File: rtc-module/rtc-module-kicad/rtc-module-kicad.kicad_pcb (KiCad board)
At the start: 2 copper layers, 45.5 x 36.4 mm, 11 parts, among them J1 Battery-holder, J2 Microcontroller, U1 PCF8563T

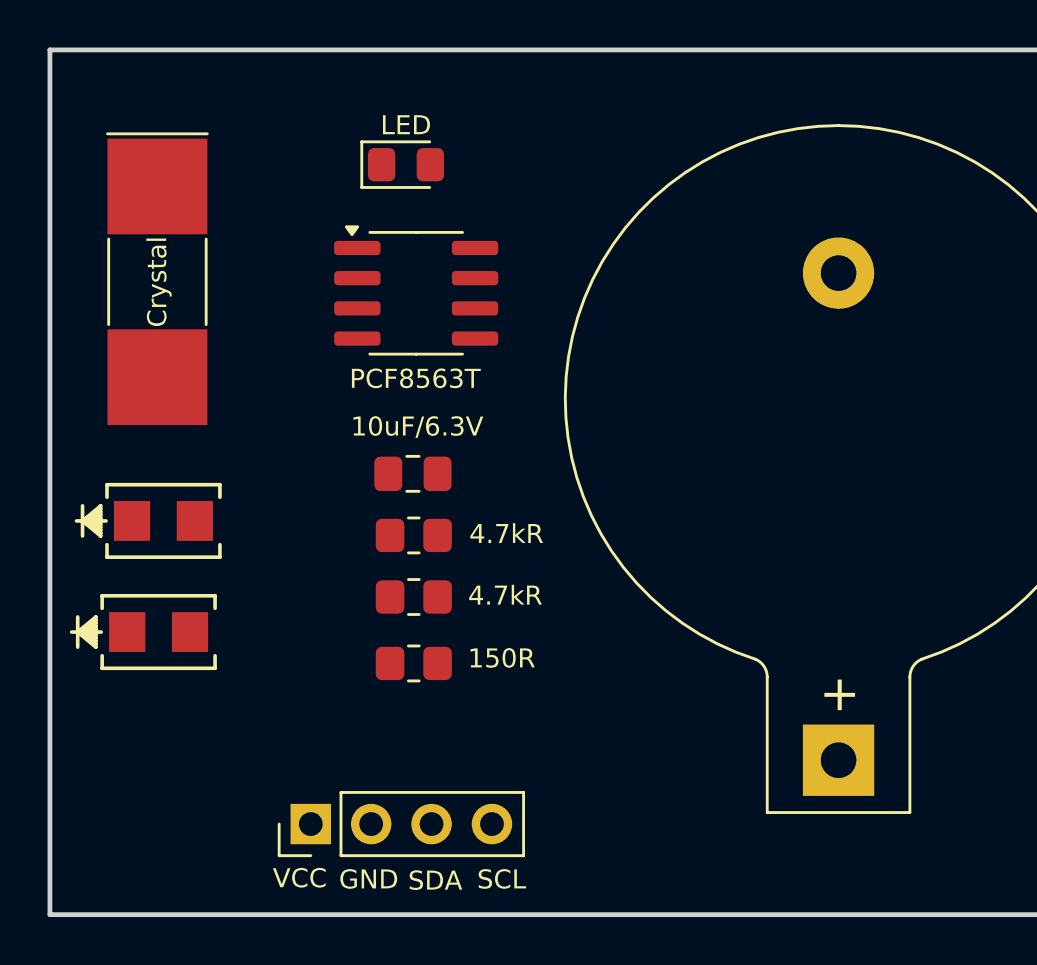
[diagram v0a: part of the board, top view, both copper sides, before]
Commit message: Connected items on the pcb.
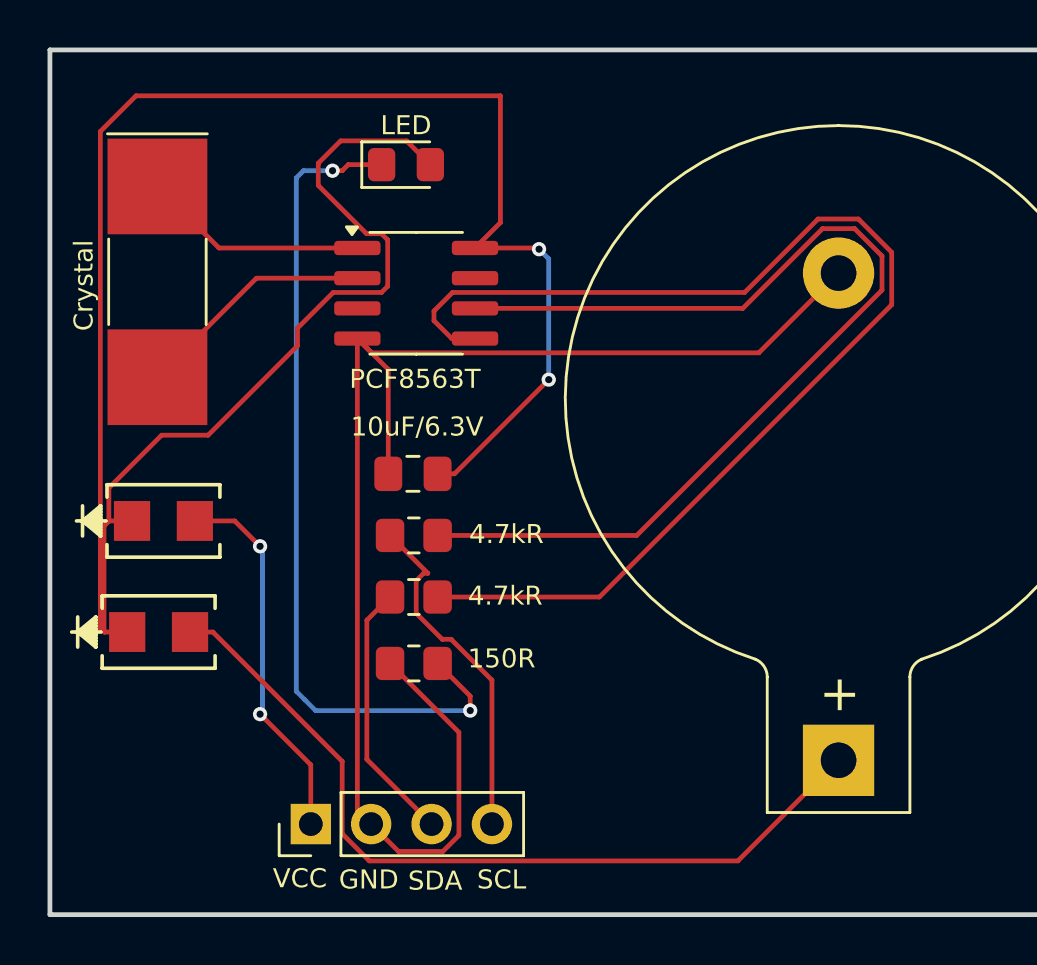
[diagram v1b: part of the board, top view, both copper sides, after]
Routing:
- net Net-(D1-K): track 0.00 -> 96.1 mm, vias 0 -> 2
- net Net-(J1-Pin_2): track 0.00 -> 61.6 mm
- net Net-(U1-SDA): track 0.00 -> 50.3 mm
- net Net-(U1-SCL): track 0.00 -> 43.4 mm
- net Net-(D3-K): track 0.00 -> 35.6 mm, vias 0 -> 2
- net Net-(D1-A): track 0.00 -> 34.8 mm
- net Net-(D2-A): track 0.00 -> 15.8 mm, vias 0 -> 2
- net Net-(J2-Pin_4): track 0.00 -> 14.6 mm
- net Net-(J2-Pin_3): track 0.00 -> 11.1 mm
- net Net-(U1-OSCO): track 0.00 -> 10.1 mm
- net Net-(U1-OSCI): track 0.00 -> 9.48 mm

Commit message: Added the gerber and drill files ready to order!
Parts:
- added 10uF/6.3V: C - 10uF/6.3V, Capacitor_SMD:C_0805_2012Metric_Pad1.18x1.45mm_HandSolder, F.Cu at (126.1, 164.4)
- added 10uF/6.3V: C - 10uF/6.3V, Capacitor_SMD:C_0805_2012Metric_Pad1.18x1.45mm_HandSolder, F.Cu at (77.9, 125.2)
- added 10uF/6.3V: C - 10uF/6.3V, Capacitor_SMD:C_0805_2012Metric_Pad1.18x1.45mm_HandSolder, F.Cu at (77.7, 86.4)
- added 10uF/6.3V: C - 10uF/6.3V, Capacitor_SMD:C_0805_2012Metric_Pad1.18x1.45mm_HandSolder, F.Cu at (125.8, 86.9)
- added 10uF/6.3V: C - 10uF/6.3V, Capacitor_SMD:C_0805_2012Metric_Pad1.18x1.45mm_HandSolder, F.Cu at (126.0, 125.6)
- added 10uF/6.3V: C - 10uF/6.3V, Capacitor_SMD:C_0805_2012Metric_Pad1.18x1.45mm_HandSolder, F.Cu at (125.7, 48.1)
- added 10uF/6.3V: C - 10uF/6.3V, Capacitor_SMD:C_0805_2012Metric_Pad1.18x1.45mm_HandSolder, F.Cu at (77.6, 47.7)
- added 150R: 150R, Resistor_SMD:R_0805_2012Metric_Pad1.20x1.40mm_HandSolder, F.Cu at (77.6, 55.6)
- added 150R: 150R, Resistor_SMD:R_0805_2012Metric_Pad1.20x1.40mm_HandSolder, F.Cu at (125.7, 56.1)
- added 150R: 150R, Resistor_SMD:R_0805_2012Metric_Pad1.20x1.40mm_HandSolder, F.Cu at (126.0, 133.6)
- added 150R: 150R, Resistor_SMD:R_0805_2012Metric_Pad1.20x1.40mm_HandSolder, F.Cu at (77.9, 133.1)
- added 150R: 150R, Resistor_SMD:R_0805_2012Metric_Pad1.20x1.40mm_HandSolder, F.Cu at (77.7, 94.4)
- added 150R: 150R, Resistor_SMD:R_0805_2012Metric_Pad1.20x1.40mm_HandSolder, F.Cu at (125.8, 94.8)
- added 150R: 150R, Resistor_SMD:R_0805_2012Metric_Pad1.20x1.40mm_HandSolder, F.Cu at (126.2, 172.4)
- added Crystal: Crystal - 32.768kHz, Crystal:Crystal_SMD_MicroCrystal_CC1V-T1A-2Pin_8.0x3.7mm_HandSoldering, F.Cu at (115.2, 117.6)
- added Crystal: Crystal - 32.768kHz, Crystal:Crystal_SMD_MicroCrystal_CC1V-T1A-2Pin_8.0x3.7mm_HandSoldering, F.Cu at (115.4, 156.3)
- added Crystal: Crystal - 32.768kHz, Crystal:Crystal_SMD_MicroCrystal_CC1V-T1A-2Pin_8.0x3.7mm_HandSoldering, F.Cu at (66.8, 39.6)
- added Crystal: Crystal - 32.768kHz, Crystal:Crystal_SMD_MicroCrystal_CC1V-T1A-2Pin_8.0x3.7mm_HandSoldering, F.Cu at (115.1, 78.8)
- added Crystal: Crystal - 32.768kHz, Crystal:Crystal_SMD_MicroCrystal_CC1V-T1A-2Pin_8.0x3.7mm_HandSoldering, F.Cu at (67.0, 78.3)
- added Crystal: Crystal - 32.768kHz, Crystal:Crystal_SMD_MicroCrystal_CC1V-T1A-2Pin_8.0x3.7mm_HandSoldering, F.Cu at (67.1, 117.1)
- added Crystal: Crystal - 32.768kHz, Crystal:Crystal_SMD_MicroCrystal_CC1V-T1A-2Pin_8.0x3.7mm_HandSoldering, F.Cu at (114.9, 40.0)
- added D1: Schottky-diode, SS14_Schottky:DO-214AC_VIS, F.Cu at (67.0, 93.1)
- added D1: Schottky-diode, SS14_Schottky:DO-214AC_VIS, F.Cu at (66.9, 54.3)
- added D1: Schottky-diode, SS14_Schottky:DO-214AC_VIS, F.Cu at (115.1, 93.5)
- added D1: Schottky-diode, SS14_Schottky:DO-214AC_VIS, F.Cu at (115.4, 171.0)
- added D1: Schottky-diode, SS14_Schottky:DO-214AC_VIS, F.Cu at (115.0, 54.8)
- added D1: Schottky-diode, SS14_Schottky:DO-214AC_VIS, F.Cu at (67.2, 131.8)
- added D1: Schottky-diode, SS14_Schottky:DO-214AC_VIS, F.Cu at (115.3, 132.3)
- added D2: Schottky-diode, SS14_Schottky:DO-214AC_VIS, F.Cu at (67.4, 127.2)
- added D2: Schottky-diode, SS14_Schottky:DO-214AC_VIS, F.Cu at (115.6, 166.4)
- added D2: Schottky-diode, SS14_Schottky:DO-214AC_VIS, F.Cu at (67.2, 88.4)
- added D2: Schottky-diode, SS14_Schottky:DO-214AC_VIS, F.Cu at (67.1, 49.6)
- added D2: Schottky-diode, SS14_Schottky:DO-214AC_VIS, F.Cu at (115.5, 127.6)
- added D2: Schottky-diode, SS14_Schottky:DO-214AC_VIS, F.Cu at (115.3, 88.8)
- added D2: Schottky-diode, SS14_Schottky:DO-214AC_VIS, F.Cu at (115.2, 50.1)
- added J1: Battery-holder, Battery:BatteryHolder_Keystone_103_1x20mm, F.Cu at (143.7, 98.9)
- added J1: Battery-holder, Battery:BatteryHolder_Keystone_103_1x20mm, F.Cu at (143.9, 137.7)
- added J1: Battery-holder, Battery:BatteryHolder_Keystone_103_1x20mm, F.Cu at (144.0, 176.4)
- added J1: Battery-holder, Battery:BatteryHolder_Keystone_103_1x20mm, F.Cu at (95.8, 137.2)
- added J1: Battery-holder, Battery:BatteryHolder_Keystone_103_1x20mm, F.Cu at (95.6, 98.5)
- added J1: Battery-holder, Battery:BatteryHolder_Keystone_103_1x20mm, F.Cu at (143.6, 60.2)
- added J1: Battery-holder, Battery:BatteryHolder_Keystone_103_1x20mm, F.Cu at (95.5, 59.7)
- added J2: Microcontroller, Connector_PinHeader_2.54mm:PinHeader_1x04_P2.54mm_Vertical, F.Cu at (73.6, 139.9)
- added J2: Microcontroller, Connector_PinHeader_2.54mm:PinHeader_1x04_P2.54mm_Vertical, F.Cu at (121.5, 101.6)
- added J2: Microcontroller, Connector_PinHeader_2.54mm:PinHeader_1x04_P2.54mm_Vertical, F.Cu at (121.4, 62.8)
- added J2: Microcontroller, Connector_PinHeader_2.54mm:PinHeader_1x04_P2.54mm_Vertical, F.Cu at (73.3, 62.4)
- added J2: Microcontroller, Connector_PinHeader_2.54mm:PinHeader_1x04_P2.54mm_Vertical, F.Cu at (121.7, 140.4)
- added J2: Microcontroller, Connector_PinHeader_2.54mm:PinHeader_1x04_P2.54mm_Vertical, F.Cu at (121.8, 179.1)
- added J2: Microcontroller, Connector_PinHeader_2.54mm:PinHeader_1x04_P2.54mm_Vertical, F.Cu at (73.4, 101.1)
- added LED: LED, LED_SMD:LED_0805_2012Metric_Pad1.15x1.40mm_HandSolder, F.Cu at (77.3, 34.6)
- added LED: LED, LED_SMD:LED_0805_2012Metric_Pad1.15x1.40mm_HandSolder, F.Cu at (125.7, 112.6)
- added LED: LED, LED_SMD:LED_0805_2012Metric_Pad1.15x1.40mm_HandSolder, F.Cu at (77.4, 73.4)
- added LED: LED, LED_SMD:LED_0805_2012Metric_Pad1.15x1.40mm_HandSolder, F.Cu at (125.5, 73.9)
- added LED: LED, LED_SMD:LED_0805_2012Metric_Pad1.15x1.40mm_HandSolder, F.Cu at (125.8, 151.4)
- added LED: LED, LED_SMD:LED_0805_2012Metric_Pad1.15x1.40mm_HandSolder, F.Cu at (125.4, 35.1)
- added LED: LED, LED_SMD:LED_0805_2012Metric_Pad1.15x1.40mm_HandSolder, F.Cu at (77.6, 112.2)
- added R1: 4.7kR, Resistor_SMD:R_0805_2012Metric_Pad1.20x1.40mm_HandSolder, F.Cu at (125.7, 53.3)
- added R1: 4.7kR, Resistor_SMD:R_0805_2012Metric_Pad1.20x1.40mm_HandSolder, F.Cu at (77.7, 91.6)
- added R1: 4.7kR, Resistor_SMD:R_0805_2012Metric_Pad1.20x1.40mm_HandSolder, F.Cu at (126.2, 169.6)
- added R1: 4.7kR, Resistor_SMD:R_0805_2012Metric_Pad1.20x1.40mm_HandSolder, F.Cu at (125.8, 92.0)
- added R1: 4.7kR, Resistor_SMD:R_0805_2012Metric_Pad1.20x1.40mm_HandSolder, F.Cu at (77.6, 52.8)
- added R1: 4.7kR, Resistor_SMD:R_0805_2012Metric_Pad1.20x1.40mm_HandSolder, F.Cu at (77.9, 130.4)
- added R1: 4.7kR, Resistor_SMD:R_0805_2012Metric_Pad1.20x1.40mm_HandSolder, F.Cu at (126.0, 130.8)
- added R2: 4.7kR, Resistor_SMD:R_0805_2012Metric_Pad1.20x1.40mm_HandSolder, F.Cu at (77.6, 50.2)
- added R2: 4.7kR, Resistor_SMD:R_0805_2012Metric_Pad1.20x1.40mm_HandSolder, F.Cu at (125.7, 50.7)
- added R2: 4.7kR, Resistor_SMD:R_0805_2012Metric_Pad1.20x1.40mm_HandSolder, F.Cu at (125.8, 89.5)
- added R2: 4.7kR, Resistor_SMD:R_0805_2012Metric_Pad1.20x1.40mm_HandSolder, F.Cu at (77.7, 89.0)
- added R2: 4.7kR, Resistor_SMD:R_0805_2012Metric_Pad1.20x1.40mm_HandSolder, F.Cu at (126.2, 167.0)
- added R2: 4.7kR, Resistor_SMD:R_0805_2012Metric_Pad1.20x1.40mm_HandSolder, F.Cu at (126.0, 128.2)
- added R2: 4.7kR, Resistor_SMD:R_0805_2012Metric_Pad1.20x1.40mm_HandSolder, F.Cu at (77.9, 127.8)
- added U1: PCF8563T, Package_SO:SOIC-8_3.9x4.9mm_P1.27mm, F.Cu at (126.3, 156.8)
- added U1: PCF8563T, Package_SO:SOIC-8_3.9x4.9mm_P1.27mm, F.Cu at (125.8, 40.5)
- added U1: PCF8563T, Package_SO:SOIC-8_3.9x4.9mm_P1.27mm, F.Cu at (78.0, 117.6)
- added U1: PCF8563T, Package_SO:SOIC-8_3.9x4.9mm_P1.27mm, F.Cu at (125.9, 79.3)
- added U1: PCF8563T, Package_SO:SOIC-8_3.9x4.9mm_P1.27mm, F.Cu at (126.1, 118.0)
- added U1: PCF8563T, Package_SO:SOIC-8_3.9x4.9mm_P1.27mm, F.Cu at (77.7, 40.1)
- added U1: PCF8563T, Package_SO:SOIC-8_3.9x4.9mm_P1.27mm, F.Cu at (77.8, 78.8)
- moved D2 82.2 mm to (67.5, 165.9)
- moved R1 82.2 mm to (78.0, 169.1)
- moved R2 82.2 mm to (78.0, 166.5)
- moved 10uF/6.3V 82.2 mm to (78.0, 163.9)
- moved 150R 82.2 mm to (78.0, 171.9)
- moved Crystal 82.2 mm to (67.3, 155.9)
- moved D1 82.2 mm to (67.3, 170.6)
- moved J1 82.2 mm to (95.9, 176.0)
- moved J2 82.2 mm to (73.7, 178.7)
- moved LED 82.2 mm to (77.7, 150.9)
- moved U1 82.2 mm to (78.1, 156.3)
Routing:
- net Net-(D1-K): track 96.1 -> 769.1 mm, vias 2 -> 16
- net Net-(J1-Pin_2): track 61.6 -> 493.2 mm
- net Net-(U1-SDA): track 50.3 -> 402.3 mm
- net Net-(U1-SCL): track 43.4 -> 347.1 mm
- net Net-(D3-K): track 35.6 -> 284.9 mm, vias 2 -> 16
- net Net-(D1-A): track 34.8 -> 278.4 mm
- net Net-(D2-A): track 15.8 -> 126.7 mm, vias 2 -> 16
- net Net-(J2-Pin_4): track 14.6 -> 117.2 mm
- net Net-(J2-Pin_3): track 11.1 -> 88.7 mm
- net Net-(U1-OSCO): track 10.1 -> 81.1 mm
- net Net-(U1-OSCI): track 9.48 -> 75.9 mm
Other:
- board size 45.5 x 36.4 mm -> 93.2 x 152.2 mm
- board text added: "Paco :3"
- board text added: "RTC-module"
